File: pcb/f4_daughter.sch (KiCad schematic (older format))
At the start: 0 parts

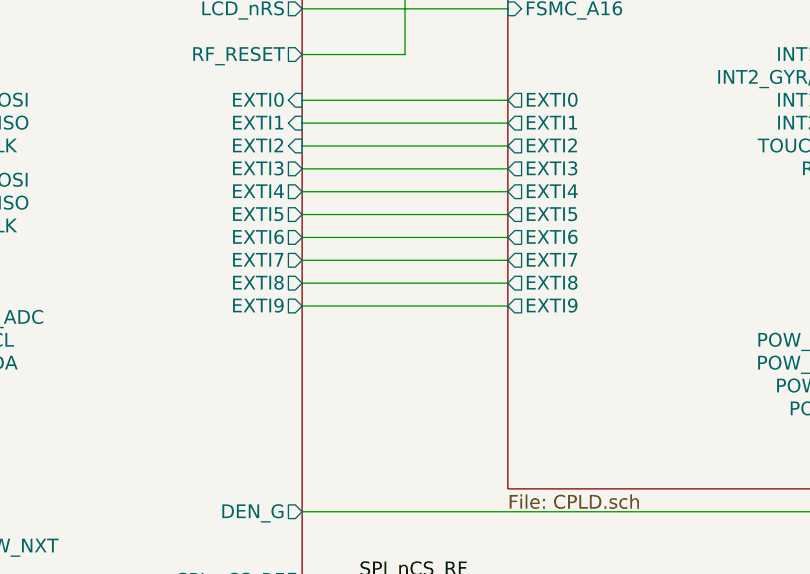
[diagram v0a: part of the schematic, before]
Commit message: CPLD connection finished.
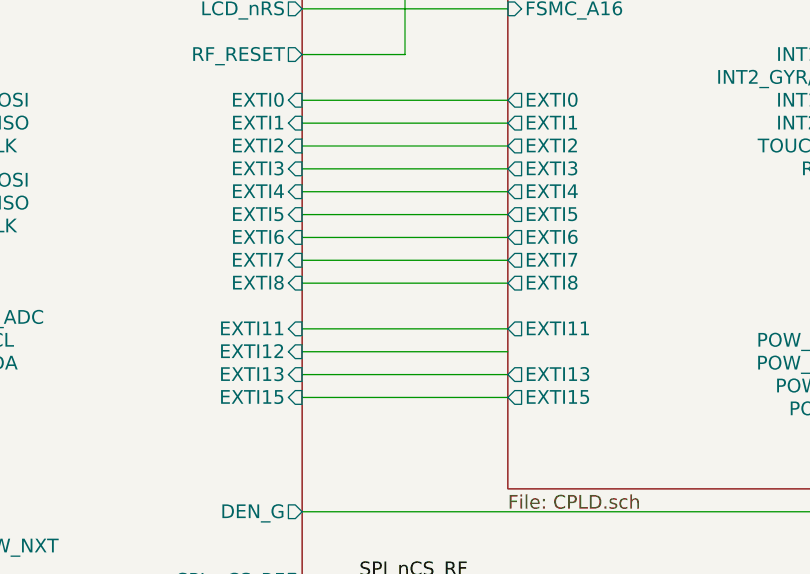
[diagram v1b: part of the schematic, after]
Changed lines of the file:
@@
-EESchema Schematic File Version 2  date 12/17/2012 11:02:29 PM
+EESchema Schematic File Version 2  date 12/19/2012 4:02:29 PM
 LIBS:power
 LIBS:device
@@
 Sheet 1 9
 Title ""
-Date "18 dec 2012"
+Date "19 dec 2012"
 Rev ""
 Comp ""
@@
 Comment4 ""
 $EndDescr
+Wire Wire Line
+	6550 4700 5650 4700
+Wire Wire Line
+	5650 4500 6550 4500
 Connection ~ 3500 6900
 Wire Wire Line
@@
 	5650 4100 6550 4100
 Wire Wire Line
-	5650 4300 6550 4300
-Wire Wire Line
 	9550 1650 9350 1650
 Wire Wire Line
@@
 Wire Wire Line
 	5650 6000 5900 6000
+Wire Wire Line
+	6550 4400 5650 4400
+Wire Wire Line
+	6550 4600 5650 4600
 Text Label 8500 2650 0    60   ~ 0
 SPI_nCS_CPLD
@@
 F5 "AUDIO_IN_R" I R 5650 7250 60
 F6 "LCD_D[0..15]" B R 5650 2500 60
-F7 "EXTI7" O R 5650 4100 60
-F8 "EXTI8" O R 5650 4200 60
-F9 "EXTI9" O R 5650 4300 60
-F10 "SPI1_MISO" I L 3950 3500 60
-F11 "POW_HPWR" O L 3950 2800 60
-F12 "POW_MODE" O L 3950 2700 60
-F13 "POW_nCHRG" I L 3950 2600 60
-F14 "EN_POW_NXT" O L 3950 5350 60
-F15 "STM32_ADC" I L 3950 4350 60
-F16 "NXT_SCL" B L 3950 4450 60
-F17 "NXT_SDA" B L 3950 4550 60
-F18 "EN_POW_9V" O L 3950 6900 60
-F19 "EXTI1" I R 5650 3500 60
-F20 "EXTI6" O R 5650 4000 60
-F21 "EXTI0" I R 5650 3400 60
-F22 "EXTI5" O R 5650 3900 60
-F23 "EXTI2" I R 5650 3600 60
-F24 "EXTI3" O R 5650 3700 60
-F25 "EXTI4" O R 5650 3800 60
-F26 "LCD_nCS" O R 5650 2800 60
-F27 "LCD_nWR" O R 5650 2900 60
-F28 "LCD_nRESET" O R 5650 2600 60
-F29 "LCD_nRS" O R 5650 3000 60
-F30 "SPI_nCS_SD" O R 5650 5600 60
-F31 "DEN_G" O R 5650 5200 60
-F32 "SPI2_MISO" I L 3950 3850 60
-F33 "SPI1_CLK" O L 3950 3600 60
-F34 "SPI1_MOSI" O L 3950 3400 60
-F35 "SPI2_MOSI" O L 3950 3750 60
-F36 "SPI2_CLK" O L 3950 3950 60
-F37 "RF_RESET" O R 5650 3200 60
-F38 "SPI_nCS_TOUCH" O R 5650 5700 60
-F39 "SPI_nCS_RF" O R 5650 5500 60
-F40 "SPI_nCS_ACC" O R 5650 5900 60
-F41 "SPI_nCS_GYR" O R 5650 5800 60
-F42 "SPI_nCS_CPLD" O R 5650 6000 60
+F7 "EXTI7" I R 5650 4100 60
+F8 "EXTI8" I R 5650 4200 60
+F9 "SPI1_MISO" I L 3950 3500 60
+F10 "POW_HPWR" O L 3950 2800 60
+F11 "POW_MODE" O L 3950 2700 60
+F12 "POW_nCHRG" I L 3950 2600 60
+F13 "EN_POW_NXT" O L 3950 5350 60
+F14 "STM32_ADC" I L 3950 4350 60
+F15 "NXT_SCL" B L 3950 4450 60
+F16 "NXT_SDA" B L 3950 4550 60
+F17 "EN_POW_9V" O L 3950 6900 60
+F18 "EXTI1" I R 5650 3500 60
+F19 "EXTI6" I R 5650 4000 60
+F20 "EXTI0" I R 5650 3400 60
+F21 "EXTI5" I R 5650 3900 60
+F22 "EXTI2" I R 5650 3600 60
+F23 "EXTI3" I R 5650 3700 60
+F24 "EXTI4" I R 5650 3800 60
+F25 "LCD_nCS" O R 5650 2800 60
+F26 "LCD_nWR" O R 5650 2900 60
+F27 "LCD_nRESET" O R 5650 2600 60
+F28 "LCD_nRS" O R 5650 3000 60
+F29 "SPI_nCS_SD" O R 5650 5600 60
+F30 "DEN_G" O R 5650 5200 60
+F31 "SPI2_MISO" I L 3950 3850 60
+F32 "SPI1_CLK" O L 3950 3600 60
+F33 "SPI1_MOSI" O L 3950 3400 60
+F34 "SPI2_MOSI" O L 3950 3750 60
+F35 "SPI2_CLK" O L 3950 3950 60
+F36 "RF_RESET" O R 5650 3200 60
+F37 "SPI_nCS_TOUCH" O R 5650 5700 60
+F38 "SPI_nCS_RF" O R 5650 5500 60
+F39 "SPI_nCS_ACC" O R 5650 5900 60
+F40 "SPI_nCS_GYR" O R 5650 5800 60
+F41 "SPI_nCS_CPLD" O R 5650 6000 60
+F42 "EXTI13" I R 5650 4600 60
+F43 "EXTI11" I R 5650 4400 60
+F44 "EXTI15" I R 5650 4700 60
+F45 "EXTI12" I R 5650 4500 60
 $EndSheet
 Text Label 8700 3600 0    60   ~ 0
@@
 F13 "EXTI4" O L 6550 3800 60
 F14 "EXTI5" O L 6550 3900 60
-F15 "EXTI9" O L 6550 4300 60
-F16 "EXTI8" O L 6550 4200 60
-F17 "EXTI7" O L 6550 4100 60
-F18 "EXTI6" O L 6550 4000 60
-F19 "SPI_MISO" O R 8200 2550 60
-F20 "SPI_NCS" I R 8200 2650 60
-F21 "SPI_MOSI" I R 8200 2450 60
-F22 "SPI_SCK" I R 8200 2350 60
-F23 "RS" O L 6550 2350 60
-F24 "nWR" O L 6550 2450 60
-F25 "nRD" O L 6550 2550 60
-F26 "nCS" O L 6550 2650 60
-F27 "TOUCH_IRQ" I R 8200 3600 60
-F28 "RF_IRQ" I R 8200 3700 60
-F29 "INT2_GYR/DRDY" I R 8200 3300 60
-F30 "INT1_GYR" I R 8200 3200 60
-F31 "INT2_ACC" I R 8200 3500 60
-F32 "INT1_ACC" I R 8200 3400 60
+F15 "EXTI8" O L 6550 4200 60
+F16 "EXTI7" O L 6550 4100 60
+F17 "EXTI6" O L 6550 4000 60
+F18 "SPI_MISO" O R 8200 2550 60
+F19 "SPI_NCS" I R 8200 2650 60
+F20 "SPI_MOSI" I R 8200 2450 60
+F21 "SPI_SCK" I R 8200 2350 60
+F22 "RS" O L 6550 2350 60
+F23 "nWR" O L 6550 2450 60
+F24 "nRD" O L 6550 2550 60
+F25 "nCS" O L 6550 2650 60
+F26 "TOUCH_IRQ" I R 8200 3600 60
+F27 "RF_IRQ" I R 8200 3700 60
+F28 "INT2_GYR/DRDY" I R 8200 3300 60
+F29 "INT1_GYR" I R 8200 3200 60
+F30 "INT2_ACC" I R 8200 3500 60
+F31 "INT1_ACC" I R 8200 3400 60
+F32 "EXTI11" O L 6550 4400 60
+F33 "EXTI13" O L 6550 4600 60
+F34 "EXTI15" O L 6550 4700 60
 $EndSheet
 Text Label 5900 5500 0    60   ~ 0

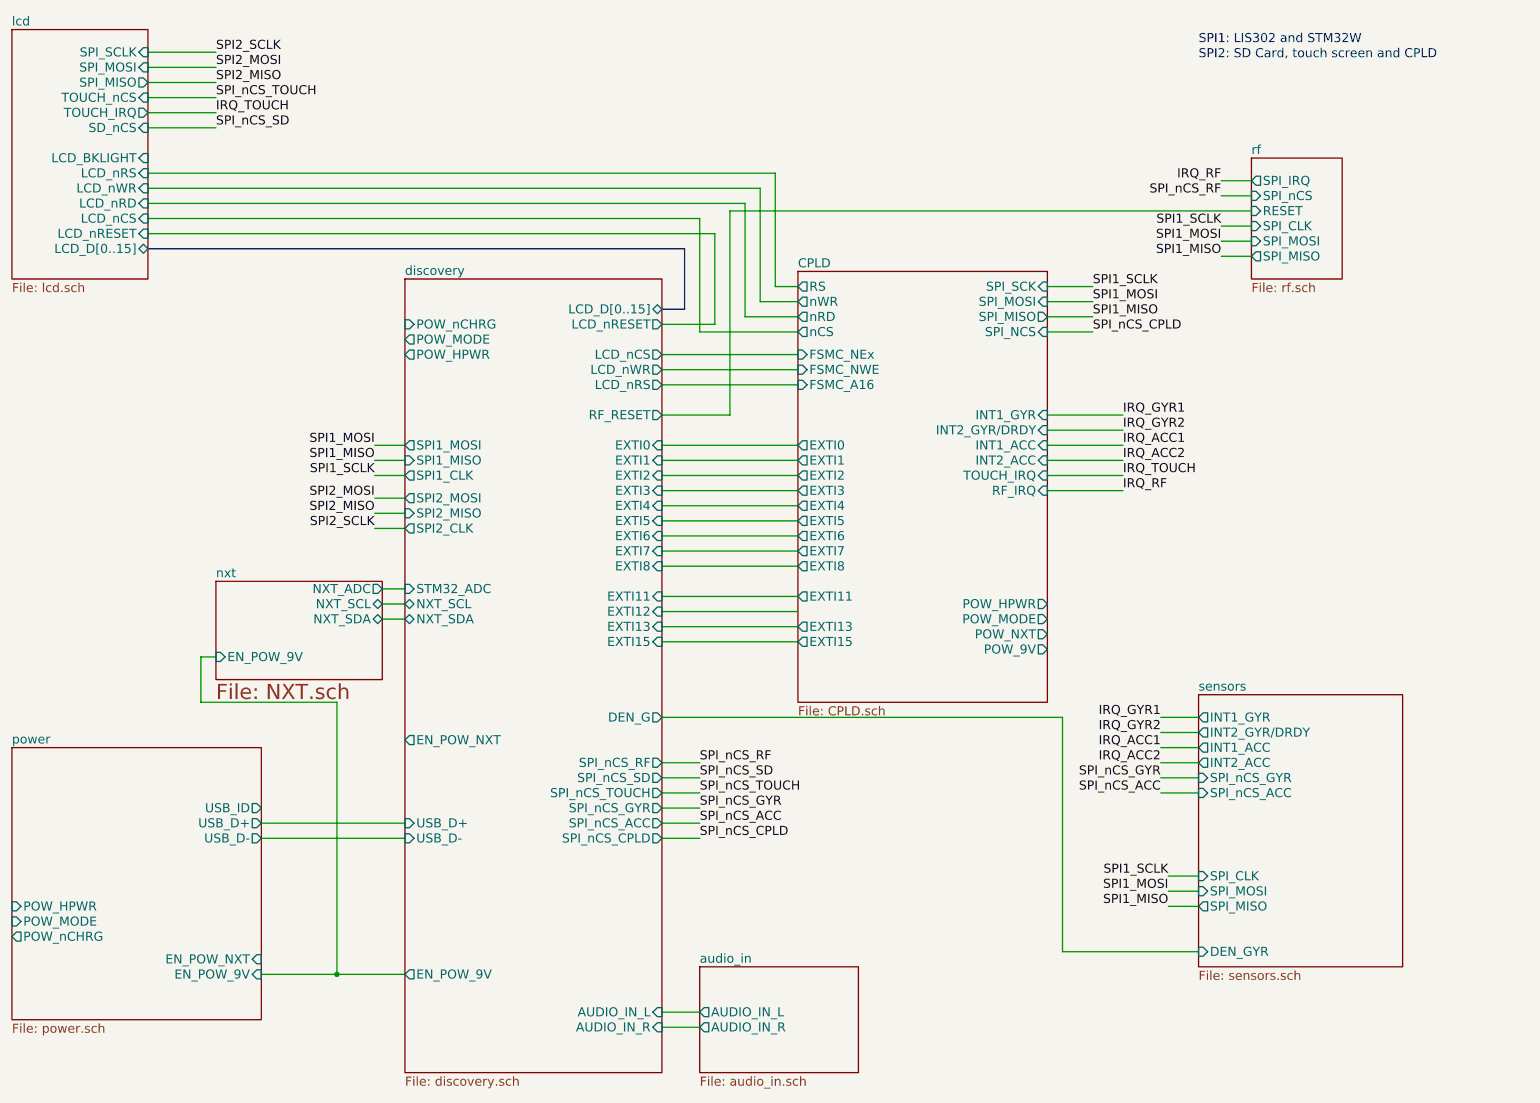
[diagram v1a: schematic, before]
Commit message: Added backlight driver, connected to I2C1, annotated stuff
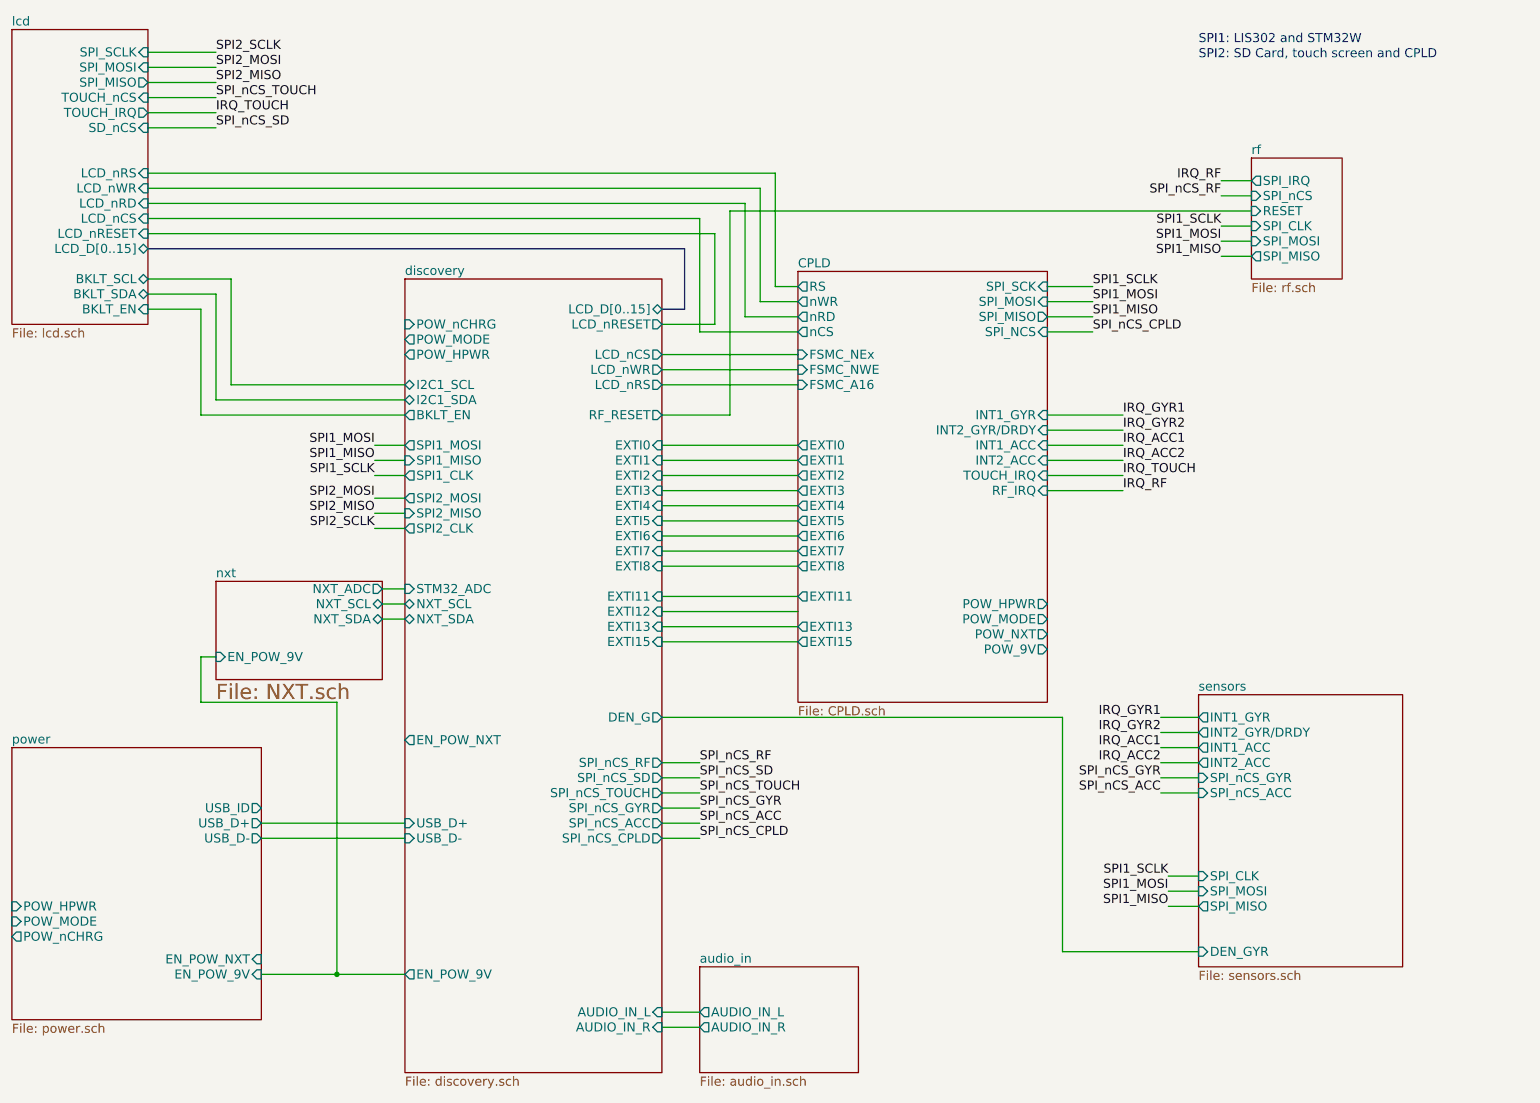
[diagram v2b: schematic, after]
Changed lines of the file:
@@
-EESchema Schematic File Version 2  date 12/19/2012 4:02:29 PM
+EESchema Schematic File Version 2  date Fri 28 Dec 2012 12:18:10 AM EST
 LIBS:power
 LIBS:device
@@
 Sheet 1 9
 Title ""
-Date "19 dec 2012"
+Date "28 dec 2012"
 Rev ""
 Comp ""
@@
 $EndDescr
 Wire Wire Line
-	6550 4700 5650 4700
-Wire Wire Line
-	5650 4500 6550 4500
-Connection ~ 3500 6900
-Wire Wire Line
-	3500 6900 3500 5100
-Wire Wire Line
-	3500 5100 2600 5100
-Wire Wire Line
-	2600 5100 2600 4800
-Wire Wire Line
-	2600 4800 2700 4800
-Wire Bus Line
-	5650 2500 5800 2500
-Wire Wire Line
-	5900 5800 5650 5800
-Wire Wire Line
-	2250 1800 6200 1800
-Wire Wire Line
-	6200 1800 6200 2550
-Wire Wire Line
-	8700 3600 8200 3600
-Wire Wire Line
-	6200 2550 6550 2550
-Wire Wire Line
-	2250 1600 6400 1600
-Wire Wire Line
-	6400 1600 6400 2350
-Wire Wire Line
-	6400 2350 6550 2350
-Wire Wire Line
-	8700 3300 8200 3300
-Wire Wire Line
-	8700 3500 8200 3500
-Wire Wire Line
-	9200 5500 8950 5500
-Wire Wire Line
-	9200 5400 8950 5400
-Wire Wire Line
-	9200 5200 8950 5200
-Wire Wire Line
-	2250 1200 2700 1200
-Wire Wire Line
-	5650 4200 6550 4200
-Wire Wire Line
-	5650 4000 6550 4000
-Wire Wire Line
-	5650 3800 6550 3800
-Wire Wire Line
-	5650 3600 6550 3600
-Wire Wire Line
-	5650 3400 6550 3400
-Wire Wire Line
-	5650 2900 6550 2900
-Wire Wire Line
-	5650 2600 6000 2600
-Wire Wire Line
-	9200 5700 8950 5700
-Wire Wire Line
-	9550 1750 9350 1750
-Wire Wire Line
-	5650 5600 5900 5600
-Wire Wire Line
-	2250 1300 2700 1300
-Wire Wire Line
-	3950 6900 3000 6900
-Wire Wire Line
-	3950 5900 3000 5900
-Wire Wire Line
-	3950 4550 3800 4550
-Wire Wire Line
-	5900 7250 5650 7250
-Wire Wire Line
-	8200 2650 8500 2650
-Wire Wire Line
-	8200 2450 8500 2450
-Wire Wire Line
-	3950 3950 3750 3950
-Wire Wire Line
-	3950 3750 3750 3750
-Wire Wire Line
-	3950 3500 3750 3500
-Wire Wire Line
-	9550 2050 9350 2050
-Wire Wire Line
-	9550 1950 9350 1950
-Wire Wire Line
-	9550 2150 9350 2150
-Wire Wire Line
-	9200 6450 9000 6450
-Wire Wire Line
-	9200 6250 9000 6250
-Wire Wire Line
-	2700 900  2250 900
-Wire Wire Line
-	2250 2000 6000 2000
-Wire Wire Line
-	6000 2000 6000 2600
-Wire Bus Line
-	2250 2100 5800 2100
+	2250 2500 2600 2500
+Wire Wire Line
+	2600 2500 2600 3200
+Wire Wire Line
+	2600 3200 3950 3200
+Wire Wire Line
+	2250 2300 2800 2300
+Wire Wire Line
+	2800 2300 2800 3000
+Wire Wire Line
+	2800 3000 3950 3000
+Wire Wire Line
+	6550 4600 5650 4600
+Wire Wire Line
+	6550 4400 5650 4400
+Wire Wire Line
+	5650 6000 5900 6000
+Wire Wire Line
+	5900 5900 5650 5900
+Wire Wire Line
+	9550 1850 6100 1850
+Wire Wire Line
+	6100 1850 6100 3200
+Wire Wire Line
+	8700 3700 8200 3700
+Wire Wire Line
+	2250 1900 5900 1900
+Wire Wire Line
+	5900 1900 5900 2650
+Wire Wire Line
+	5900 2650 6550 2650
+Wire Wire Line
+	2250 1700 6300 1700
+Wire Wire Line
+	6300 1700 6300 2450
+Wire Wire Line
+	6300 2450 6550 2450
+Wire Wire Line
+	5650 2800 6550 2800
+Wire Wire Line
+	8700 3200 8200 3200
+Wire Wire Line
+	8700 3400 8200 3400
+Wire Wire Line
+	5650 5200 8300 5200
+Wire Wire Line
+	8300 5200 8300 6750
+Wire Wire Line
+	8300 6750 9200 6750
+Wire Wire Line
+	9200 5300 8950 5300
+Wire Wire Line
+	9550 1650 9350 1650
+Wire Wire Line
+	5650 4100 6550 4100
+Wire Wire Line
+	5650 3900 6550 3900
+Wire Wire Line
+	5650 3700 6550 3700
+Wire Wire Line
+	5650 3500 6550 3500
+Wire Wire Line
+	5650 3000 6550 3000
+Wire Wire Line
+	6100 3200 5650 3200
+Wire Wire Line
+	9200 5600 8950 5600
+Wire Wire Line
+	5650 5700 5900 5700
+Wire Wire Line
+	5650 5500 5900 5500
+Wire Wire Line
+	2250 1100 2700 1100
+Wire Wire Line
+	3950 6000 3000 6000
+Wire Wire Line
+	3950 4350 3800 4350
+Wire Wire Line
+	3950 4450 3800 4450
+Wire Wire Line
+	5900 7150 5650 7150
+Wire Wire Line
+	8200 2550 8500 2550
+Wire Wire Line
+	8500 2350 8200 2350
+Wire Wire Line
+	3950 3850 3750 3850
+Wire Wire Line
+	3950 3600 3750 3600
+Wire Wire Line
+	3950 3400 3750 3400
+Wire Wire Line
+	9200 6350 9000 6350
+Wire Wire Line
+	2700 800  2250 800
+Wire Wire Line
+	2700 1000 2250 1000
 Wire Bus Line
 	5800 2100 5800 2500
-Wire Wire Line
-	2700 1000 2250 1000
-Wire Wire Line
-	2700 800  2250 800
-Wire Wire Line
-	9200 6350 9000 6350
-Wire Wire Line
-	3950 3400 3750 3400
-Wire Wire Line
-	3950 3600 3750 3600
-Wire Wire Line
-	3950 3850 3750 3850
-Wire Wire Line
-	8500 2350 8200 2350
-Wire Wire Line
-	8200 2550 8500 2550
-Wire Wire Line
-	5900 7150 5650 7150
-Wire Wire Line
-	3950 4450 3800 4450
-Wire Wire Line
-	3950 4350 3800 4350
-Wire Wire Line
-	3950 6000 3000 6000
-Wire Wire Line
-	2250 1100 2700 1100
-Wire Wire Line
-	5650 5500 5900 5500
-Wire Wire Line
-	5650 5700 5900 5700
-Wire Wire Line
-	9200 5600 8950 5600
-Wire Wire Line
-	5650 3200 6100 3200
-Wire Wire Line
-	5650 3000 6550 3000
-Wire Wire Line
-	5650 3500 6550 3500
-Wire Wire Line
-	5650 3700 6550 3700
-Wire Wire Line
-	5650 3900 6550 3900
-Wire Wire Line
-	5650 4100 6550 4100
-Wire Wire Line
-	9550 1650 9350 1650
-Wire Wire Line
-	9200 5300 8950 5300
-Wire Wire Line
-	9200 6750 8300 6750
-Wire Wire Line
-	8300 6750 8300 5200
-Wire Wire Line
-	8300 5200 5650 5200
-Wire Wire Line
-	8700 3400 8200 3400
-Wire Wire Line
-	8700 3200 8200 3200
-Wire Wire Line
-	5650 2800 6550 2800
-Wire Wire Line
-	6550 2450 6300 2450
-Wire Wire Line
-	6300 2450 6300 1700
-Wire Wire Line
-	6300 1700 2250 1700
-Wire Wire Line
-	6550 2650 5900 2650
-Wire Wire Line
-	5900 2650 5900 1900
-Wire Wire Line
-	5900 1900 2250 1900
-Wire Wire Line
-	8700 3700 8200 3700
-Wire Wire Line
-	6100 3200 6100 1850
-Wire Wire Line
-	6100 1850 9550 1850
-Wire Wire Line
-	5900 5900 5650 5900
-Wire Wire Line
-	5650 6000 5900 6000
-Wire Wire Line
-	6550 4400 5650 4400
-Wire Wire Line
-	6550 4600 5650 4600
+Wire Bus Line
+	5800 2100 2250 2100
+Wire Wire Line
+	6000 2000 6000 2600
+Wire Wire Line
+	6000 2000 2250 2000
+Wire Wire Line
+	2700 900  2250 900
+Wire Wire Line
+	9200 6250 9000 6250
+Wire Wire Line
+	9200 6450 9000 6450
+Wire Wire Line
+	9550 2150 9350 2150
+Wire Wire Line
+	9550 1950 9350 1950
+Wire Wire Line
+	9550 2050 9350 2050
+Wire Wire Line
+	3950 3500 3750 3500
+Wire Wire Line
+	3950 3750 3750 3750
+Wire Wire Line
+	3950 3950 3750 3950
+Wire Wire Line
+	8200 2450 8500 2450
+Wire Wire Line
+	8200 2650 8500 2650
+Wire Wire Line
+	5900 7250 5650 7250
+Wire Wire Line
+	3950 4550 3800 4550
+Wire Wire Line
+	3950 5900 3000 5900
+Wire Wire Line
+	3950 6900 3000 6900
+Wire Wire Line
+	2250 1300 2700 1300
+Wire Wire Line
+	5650 5600 5900 5600
+Wire Wire Line
+	9550 1750 9350 1750
+Wire Wire Line
+	9200 5700 8950 5700
+Wire Wire Line
+	6000 2600 5650 2600
+Wire Wire Line
+	5650 2900 6550 2900
+Wire Wire Line
+	5650 3400 6550 3400
+Wire Wire Line
+	5650 3600 6550 3600
+Wire Wire Line
+	5650 3800 6550 3800
+Wire Wire Line
+	5650 4000 6550 4000
+Wire Wire Line
+	5650 4200 6550 4200
+Wire Wire Line
+	2250 1200 2700 1200
+Wire Wire Line
+	9200 5200 8950 5200
+Wire Wire Line
+	9200 5400 8950 5400
+Wire Wire Line
+	9200 5500 8950 5500
+Wire Wire Line
+	8700 3500 8200 3500
+Wire Wire Line
+	8700 3300 8200 3300
+Wire Wire Line
+	6550 2350 6400 2350
+Wire Wire Line
+	6400 2350 6400 1600
+Wire Wire Line
+	6400 1600 2250 1600
+Wire Wire Line
+	6550 2550 6200 2550
+Wire Wire Line
+	8700 3600 8200 3600
+Wire Wire Line
+	6200 2550 6200 1800
+Wire Wire Line
+	6200 1800 2250 1800
+Wire Wire Line
+	5900 5800 5650 5800
+Wire Bus Line
+	5800 2500 5650 2500
+Wire Wire Line
+	2700 4800 2600 4800
+Wire Wire Line
+	2600 4800 2600 5100
+Wire Wire Line
+	2600 5100 3500 5100
+Wire Wire Line
+	3500 5100 3500 6900
+Connection ~ 3500 6900
+Wire Wire Line
+	5650 4500 6550 4500
+Wire Wire Line
+	6550 4700 5650 4700
+Wire Wire Line
+	2250 2400 2700 2400
+Wire Wire Line
+	2700 2400 2700 3100
+Wire Wire Line
+	2700 3100 3950 3100
 Text Label 8500 2650 0    60   ~ 0
 SPI_nCS_CPLD
@@
 F44 "EXTI15" I R 5650 4700 60
 F45 "EXTI12" I R 5650 4500 60
+F46 "BKLT_EN" O L 3950 3200 60
+F47 "I2C1_SCL" B L 3950 3000 60
+F48 "I2C1_SDA" B L 3950 3100 60
 $EndSheet
 Text Label 8700 3600 0    60   ~ 0
@@
 $EndSheet
 $Sheet
-S 1350 650  900  1650
+S 1350 650  900  1950
 U 50188B6E
 F0 "lcd" 60
@@
 F12 "SPI_MOSI" I R 2250 900 60
 F13 "SPI_MISO" O R 2250 1000 60
-F14 "LCD_BKLIGHT" I R 2250 1500 60
+F14 "BKLT_SCL" B R 2250 2300 60
+F15 "BKLT_SDA" B R 2250 2400 60
+F16 "BKLT_EN" I R 2250 2500 60
 $EndSheet
 $Sheet
